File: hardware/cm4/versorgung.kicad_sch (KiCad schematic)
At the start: 7 parts, among them J10 USB-C 5V/USB, U10 USBLC6-2SC6

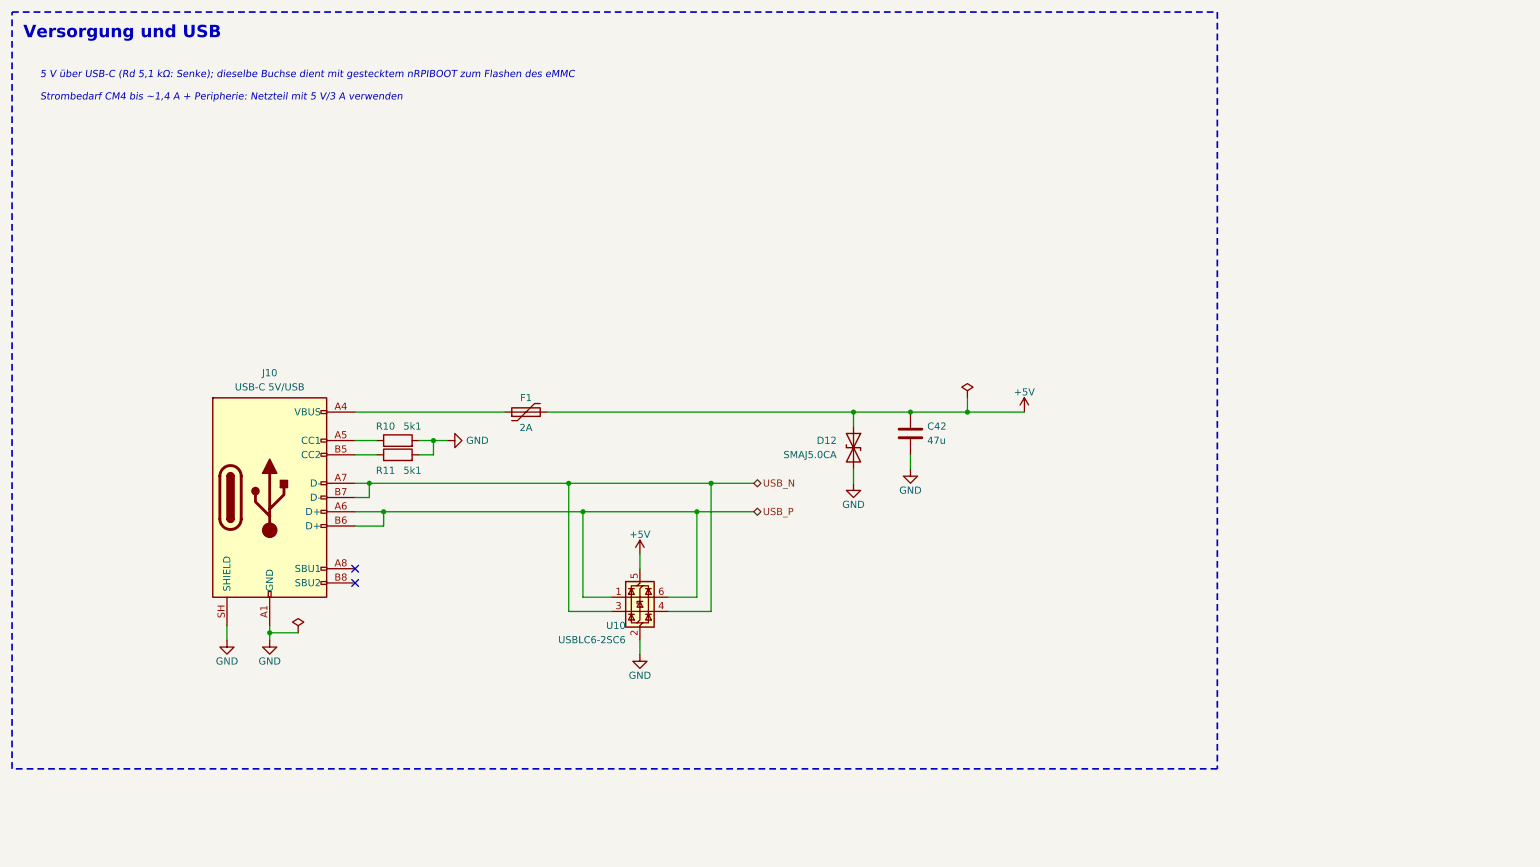
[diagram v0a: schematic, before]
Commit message: CM4-Schaltplan: Einzelblock-Blätter ohne Rahmen, Inhalt zentriert
kicadgen: Steht nur ein Block auf einem Blatt, entfällt der Rahmen (sein Titel wird
Blatttitel) und der Inhalt wird auf dem Blatt zentriert (über dem Schriftfeld, auf dem
1,27-mm-Raster). Hinweistexte der CM4-Blätter an die Schaltungen gerückt.

Co-Authored-By: Claude Opus 5.5 <noreply@anthropic.com>
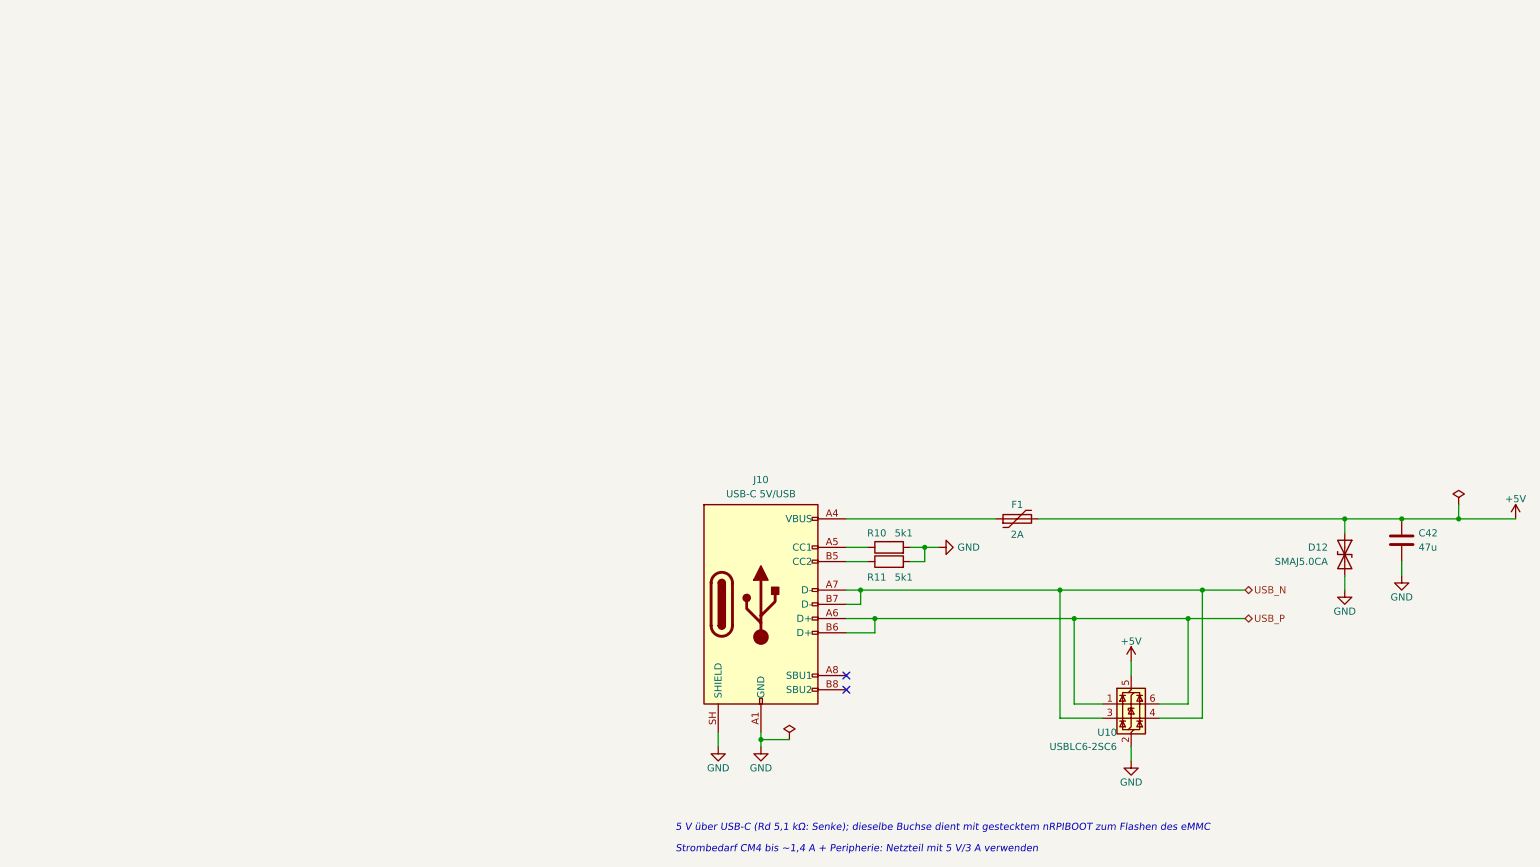
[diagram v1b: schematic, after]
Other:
- note removed: "Versorgung und USB"
- title: Versorgung -> Versorgung und USB
